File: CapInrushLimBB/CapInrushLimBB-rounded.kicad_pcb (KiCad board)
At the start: 2 copper layers, 56.5 x 34.9 mm, 29 parts, among them J1 Screw_Terminal_01x02, J2 Screw_Terminal_01x02, K1 G5LE-1A, Q1 MPSA42, Q2 IRF9540N, Q3 MPSA42, Q4 BSP230 300V 0.21A

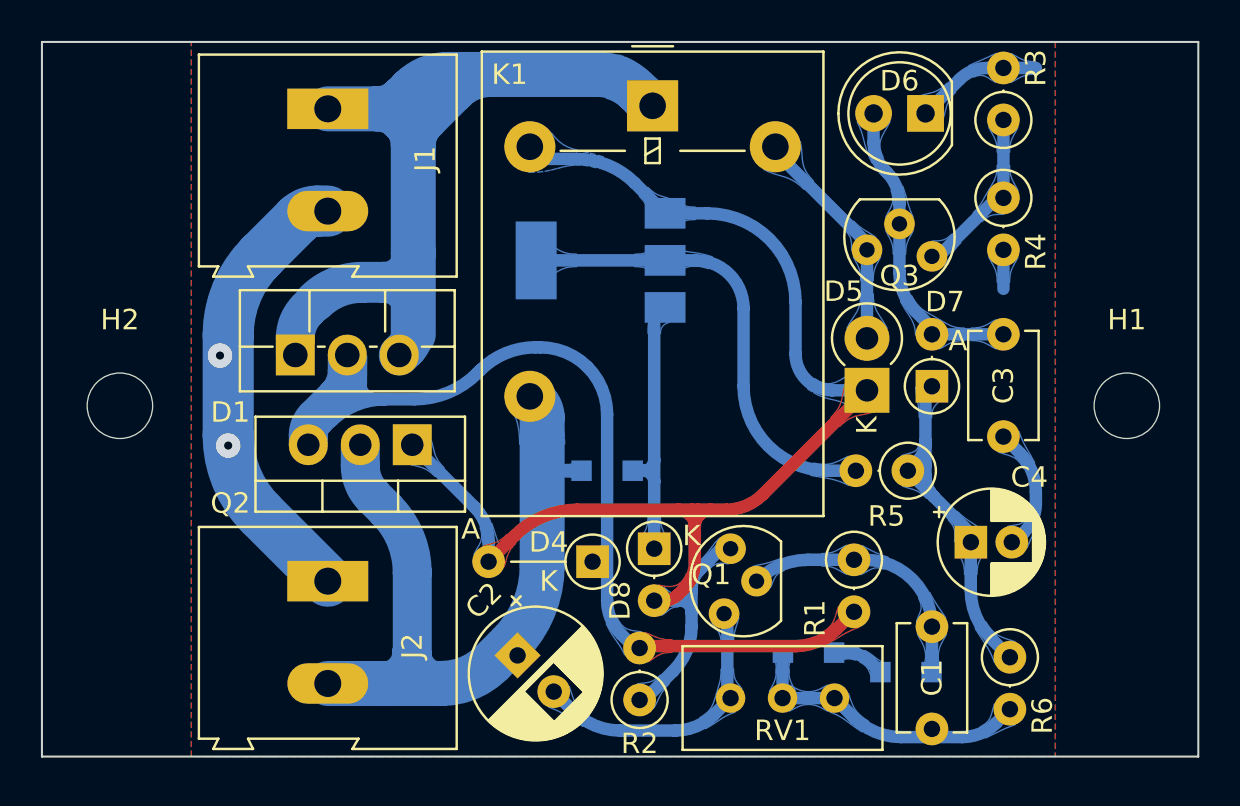
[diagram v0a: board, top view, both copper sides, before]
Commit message: Updated PCB layout of lower voltage capable inrush limiter.
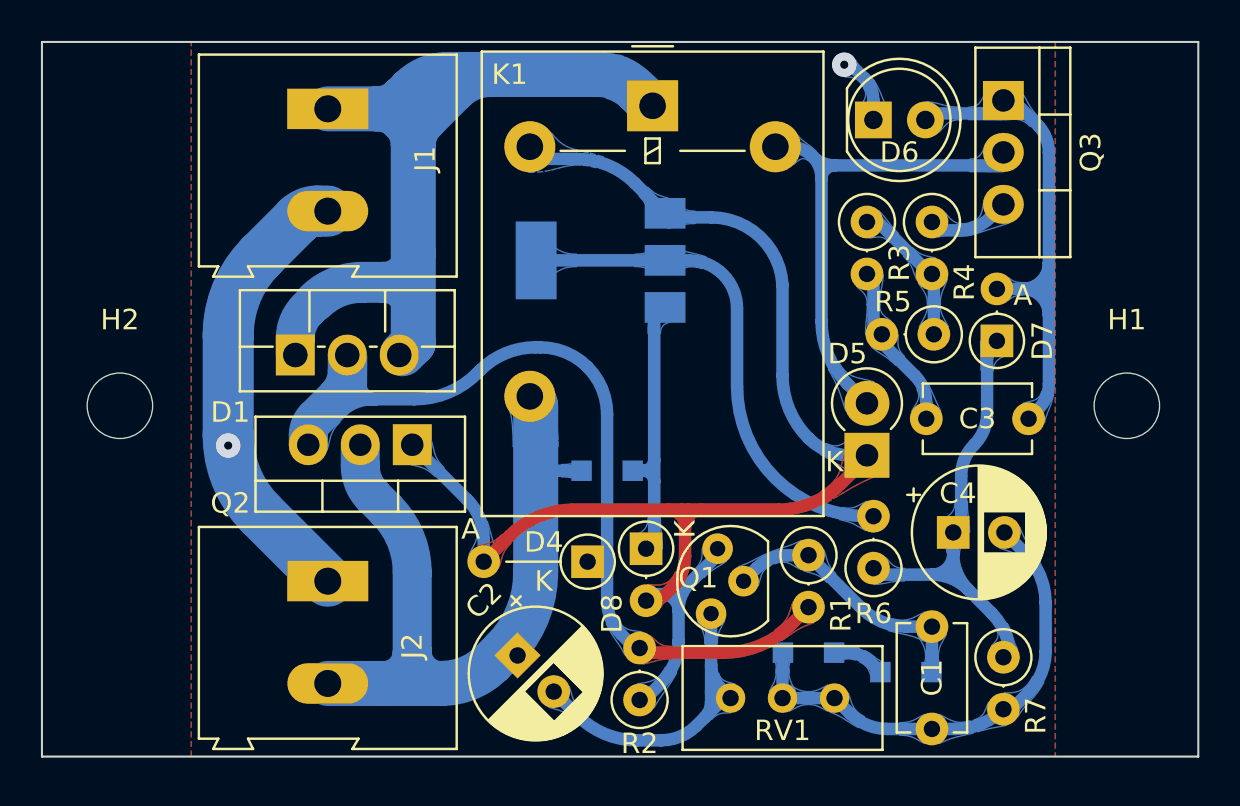
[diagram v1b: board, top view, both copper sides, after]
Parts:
- added R4: 0R, Resistor_THT:R_Axial_DIN0207_L6.3mm_D2.5mm_P2.54mm_Vertical, F.Cu at (250.5, 134.2)
- C4: value 10uF 63V -> 100uF 35V; footprint Capacitor_THT:CP_Radial_D5.0mm_P2.00mm -> Capacitor_THT:CP_Radial_D6.3mm_P2.50mm
- Q3: value MPSA42 -> TIP41C; footprint CapInrushLim:TO-92_Inline -> Package_TO_SOT_THT:TO-220-3_Vertical
- R1: value 100k -> 43k
- R3: value 1k5 -> 220R
- R5: renamed from R4; value 100R -> 110R
- R6: renamed from R5; value 100k -> 10k
- R7: renamed from R6; value 200k -> 100k
- moved R3 8.33 mm to (247.3, 134.2), turned to -90 degrees
- moved Q3 7.68 mm to (254.0, 128.3), turned to -90 degrees
- moved R5 7.48 mm to (250.6, 139.7), turned to 180 degrees
- moved R6 5.05 mm to (247.7, 151.1), turned to 90 degrees
- moved D7 3.87 mm to (253.7, 140.0)
- moved C3 3.87 mm to (250.2, 143.8), turned to 0 degrees
- moved D5 3.18 mm to (247.3, 145.6)
- moved D6 2.57 mm to (247.6, 129.2), turned to 0 degrees
- moved R1 2.23 mm to (244.5, 150.5)
- moved C4 0.99 mm to (251.5, 149.4)
- moved Q1 0.64 mm to (240.7, 153.0)
- moved D8 0.40 mm to (236.5, 150.2)
- moved R7 0.32 mm to (254.0, 155.5)
- moved D4 0.24 mm to (233.7, 150.8)
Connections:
- Q3 pad 1: Net-(Q3-Pad1) -> Net-(C3-Pad2)
- Q3 pad 2: Net-(C3-Pad2) -> /RLCoilLow
- Q3 pad 3: /RLCoilLow -> Net-(Q3-Pad3)
- R3 pad 1: Net-(Q3-Pad1) -> Net-(R3-Pad1)
- R5 pad 1: Net-(Q3-Pad1) -> Net-(R3-Pad1)
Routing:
- net /RLCoilLow: track 11.2 -> 25.8 mm
- net Net-(C3-Pad2): track 14.4 -> 27.1 mm
- net Net-(Q3-Pad1): track 8.37 -> 0.00 mm
- net Net-(R3-Pad1): track 0.00 -> 6.97 mm
- net /Gnd: track 50.9 -> 56.9 mm
- net Net-(C4-Pad1): track 18.8 -> 23.3 mm
- net Net-(Q3-Pad3): track 0.00 -> 4.23 mm
- net Net-(C2-Pad2): track 14.0 -> 18.1 mm
- net Net-(Q4-Pad2): track 22.9 -> 24.6 mm
- net /RLCoilHigh: track 72.7 -> 74.0 mm
- net /RL_Input: track 50.8 -> 49.6 mm
- net /RL_Output: track 38.2 -> 39.1 mm

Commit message: Updated layout and rounded tracks version.
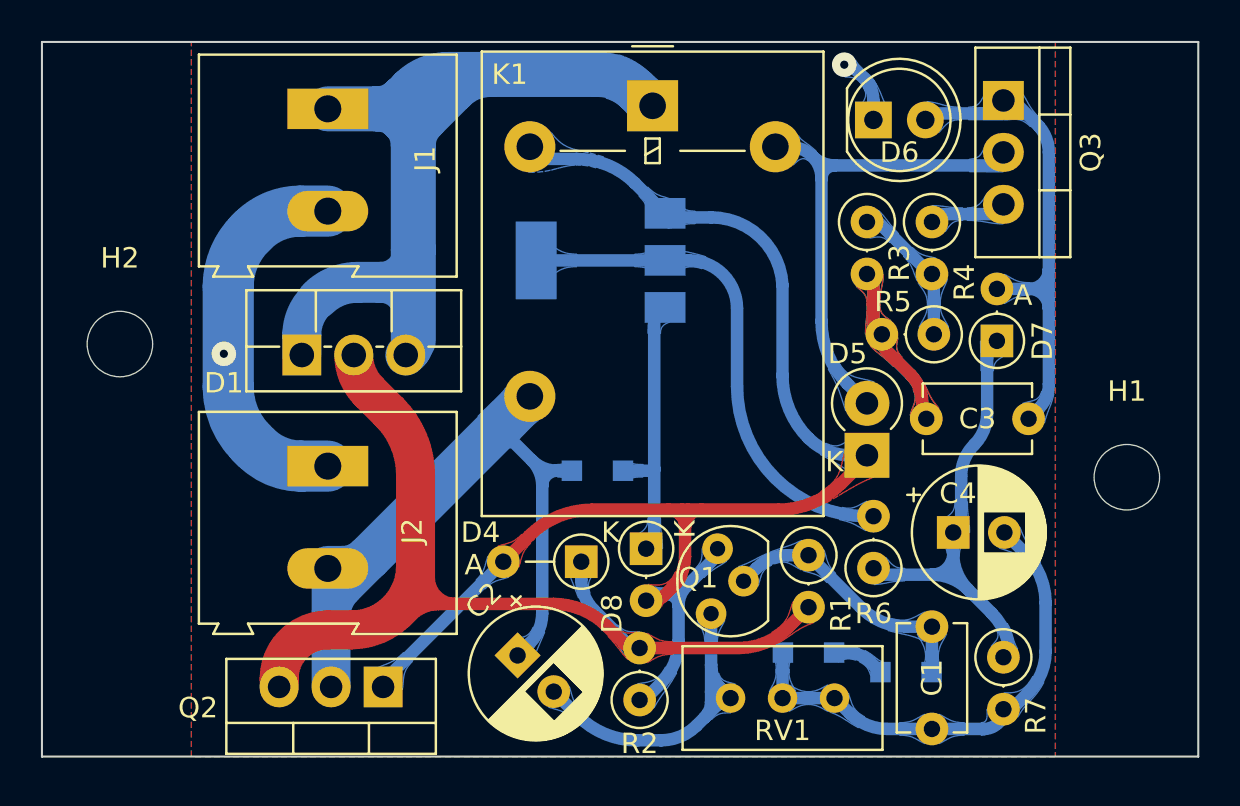
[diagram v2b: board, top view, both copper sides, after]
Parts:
- D4: footprint Diode_THT:D_DO-35_SOD27_P5.08mm_Vertical_AnodeUp -> Diode_THT:D_DO-35_SOD27_P3.81mm_Vertical_AnodeUp
- moved Q2 11.9 mm to (223.7, 156.9)
- moved J2 5.62 mm to (221.0, 146.1)
- moved H1 3.49 mm to (260.0, 146.7)
- moved H2 3.02 mm to (210.8, 140.2)
- moved D9 0.47 mm to (234.2, 146.4)
- moved D1 0.32 mm to (219.7, 140.7)
- moved D4 0.31 mm to (233.4, 150.8)
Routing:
- net /Gnd: track 56.9 -> 61.5 mm
- net /PolProtect: track 49.7 -> 52.4 mm
- net Net-(C3-Pad2): track 27.1 -> 24.5 mm
- net /RL_Input: track 49.6 -> 51.1 mm
- net /RL_Output: track 39.1 -> 40.0 mm
- net Net-(Q3-Pad3): track 4.23 -> 3.50 mm
- net Net-(D8-Pad1): track 14.1 -> 13.6 mm

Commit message: Changed the reference type, changed current set resistor strategy and updated PCB.
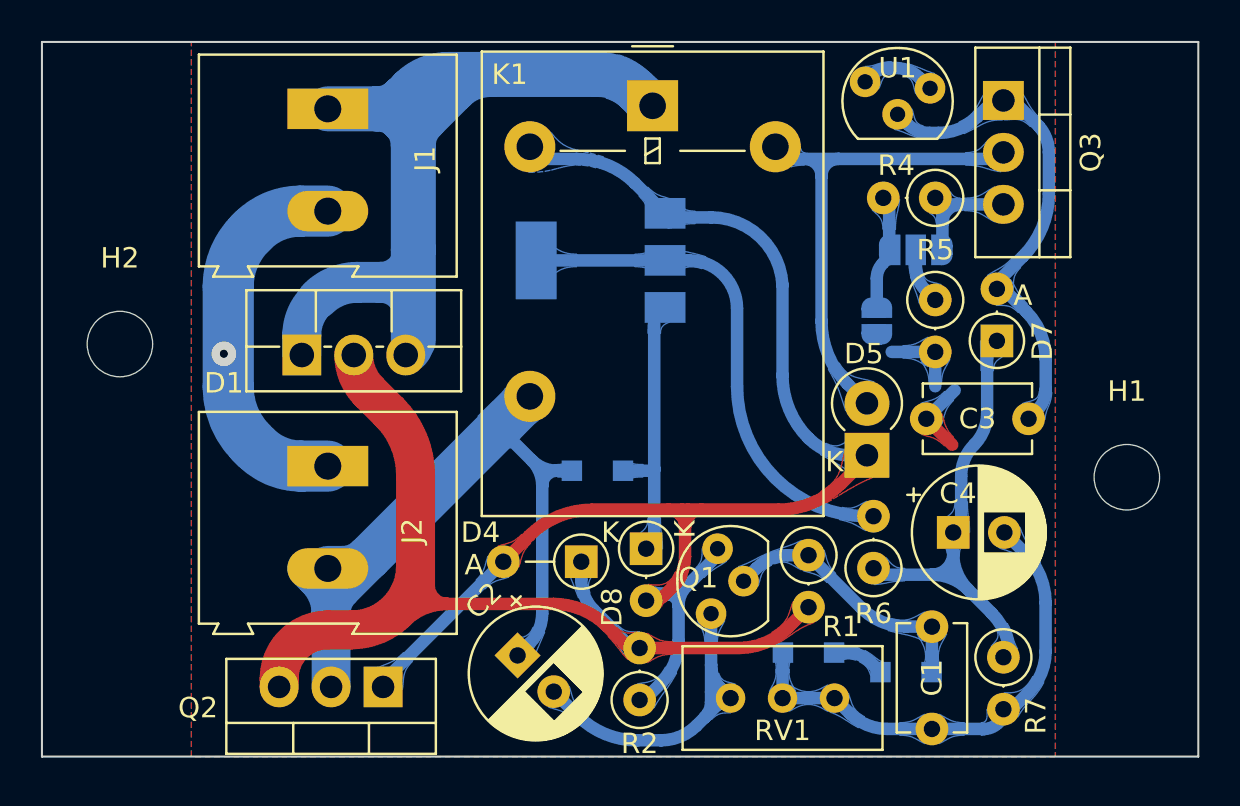
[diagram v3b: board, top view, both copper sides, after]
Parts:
- removed D6: Red LED, LED_THT:LED_D5.0mm
- removed R3: 220R, Resistor_THT:R_Axial_DIN0207_L6.3mm_D2.5mm_P2.54mm_Vertical
- added JP1: SolderJumper_3_Open, Jumper:SolderJumper-3_P1.3mm_Open_RoundedPad1.0x1.5mm, B.Cu at (249.7, 135.6)
- added JP2: SolderJumper_2_Open, Jumper:SolderJumper-2_P1.3mm_Open_RoundedPad1.0x1.5mm, B.Cu at (247.8, 139.1)
- added U1: LM385Z-ADJ, CapInrushLim:TO-92_Inline, F.Cu at (247.6, 128.3)
- R4: value 0R -> 47
- R5: value 110R -> 47
- moved R5 1.68 mm to (250.7, 138.0), turned to -90 degrees
- moved R4 1.19 mm to (250.7, 133.0), turned to 180 degrees
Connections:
- R4 pad 2: Net-(R3-Pad1) -> Net-(JP1-Pad1)
- R5 pad 1: Net-(R3-Pad1) -> Net-(JP1-Pad2)
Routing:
- net /Gnd: track 61.5 -> 54.5 mm, vias 2 -> 1
- net Net-(R3-Pad1): track 6.97 -> 0.00 mm
- net Net-(JP1-Pad1): track 0.00 -> 5.23 mm
- net Net-(JP1-Pad3): track 3.50 -> 7.04 mm
- net Net-(JP1-Pad2): track 0.00 -> 2.76 mm
- net /RL_Output: track 40.0 -> 38.8 mm
- net Net-(C3-Pad2): track 24.5 -> 23.9 mm

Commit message: Updated rounded tracks version.
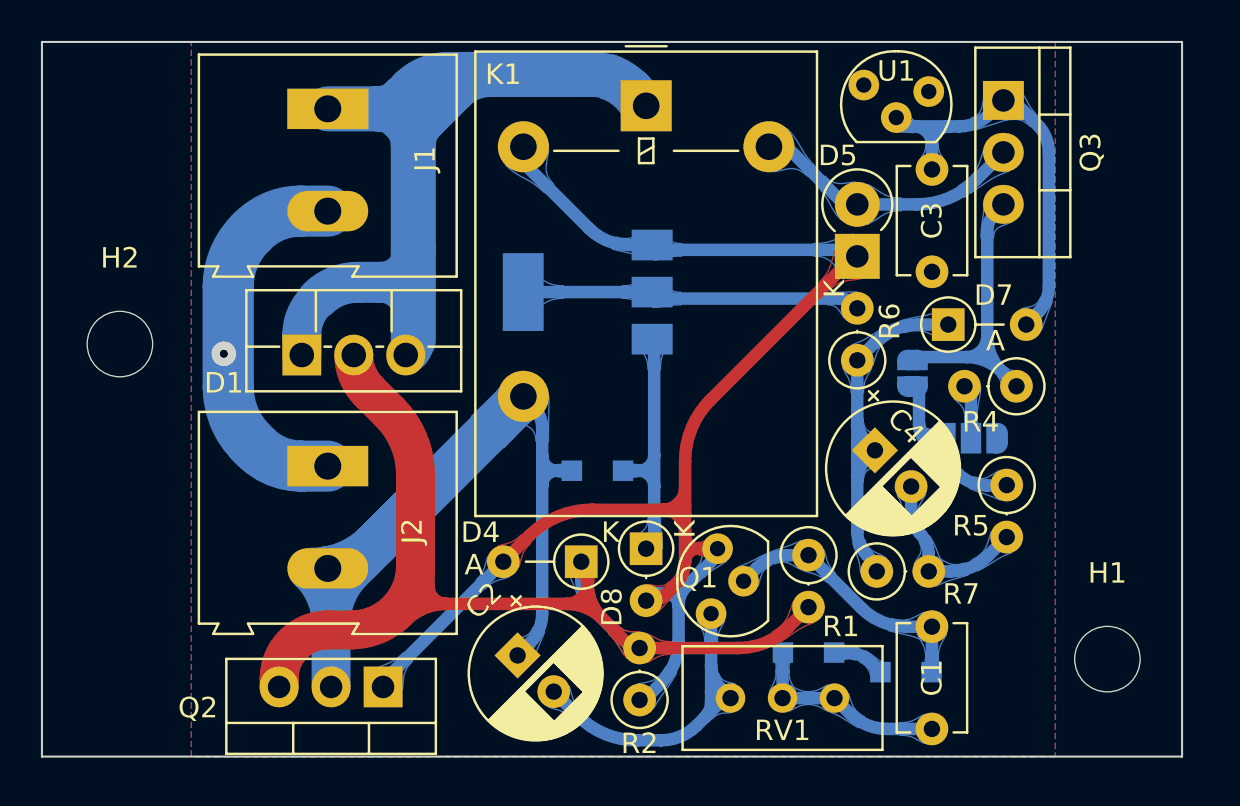
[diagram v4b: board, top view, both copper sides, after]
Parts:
- D7: footprint Diode_THT:D_DO-35_SOD27_P2.54mm_Vertical_AnodeUp -> Diode_THT:D_DO-35_SOD27_P3.81mm_Vertical_AnodeUp
- moved R6 10.2 mm to (246.9, 141.0)
- moved R4 10.0 mm to (254.6, 142.2)
- moved D5 9.73 mm to (246.9, 135.9)
- moved R5 9.70 mm to (254.2, 147.1)
- moved JP1 9.59 mm to (252.4, 144.8)
- moved H1 8.94 mm to (259.1, 155.6)
- moved R7 7.48 mm to (247.8, 151.3), turned to 0 degrees
- moved C3 7.19 mm to (250.5, 136.6), turned to 90 degrees
- moved C4 5.54 mm to (247.7, 145.4), turned to -45 degrees
- moved JP2 3.09 mm to (249.6, 141.6), turned to -90 degrees
- moved D7 2.51 mm to (251.3, 139.2), turned to 0 degrees
- moved Q4 1.67 mm to (233.7, 137.6)
- moved K1 0.31 mm to (236.5, 128.5)
- moved U1 0.17 mm to (247.5, 128.5)
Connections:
- JP1 pad 3: Net-(JP1-Pad3) -> /Gnd
- JP2 pad 1: /Gnd -> Net-(JP2-Pad1)
- Q3 pad 3: Net-(JP1-Pad3) -> Net-(JP2-Pad1)
- R4 pad 1: Net-(JP1-Pad3) -> Net-(JP2-Pad1)
- R4 pad 2: Net-(JP1-Pad1) -> Net-(JP1-Pad2)
- R5 pad 1: Net-(JP1-Pad2) -> Net-(JP1-Pad1)
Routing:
- net /Gnd: track 54.5 -> 37.7 mm
- net Net-(JP2-Pad1): track 0.00 -> 15.8 mm
- net /RLCoilLow: track 25.8 -> 12.2 mm
- net /RL_Output: track 38.8 -> 50.1 mm
- net Net-(Q4-Pad2): track 24.6 -> 16.0 mm
- net Net-(JP1-Pad3): track 7.04 -> 0.00 mm
- net Net-(JP1-Pad1): track 5.23 -> 10.3 mm
- net /PolProtect: track 52.9 -> 57.2 mm
- net Net-(C4-Pad1): track 23.3 -> 20.0 mm
- net Net-(C3-Pad2): track 23.9 -> 21.5 mm
- net /RLCoilHigh: track 74.1 -> 75.8 mm
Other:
- board size 56.5 x 34.9 mm -> 55.7 x 34.9 mm

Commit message: Updated values of relay current limiter resistors.
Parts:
- R4: value 47 -> 560
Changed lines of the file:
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@@
       (effects (font (size 1 1) (thickness 0.15)))
     )
-    (fp_text value "47" (at 1.27 2.37) (layer "F.Fab")
+    (fp_text value "560" (at 1.27 2.37) (layer "F.Fab")
       (effects (font (size 1 1) (thickness 0.15)))
     )

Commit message: Updating model, schematic and PCB to remove cap. on the relay timer ref. and to fit a zener across the relay coil.
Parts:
- C3: value 100nF 50V -> 100nF 50V (DNF)
- D5: value 1n4002 -> 1N4749A (24V)
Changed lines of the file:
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@@
       (effects (font (size 1 1) (thickness 0.15)))
     )
-    (fp_text value "1n4002" (at 1.27 3.639635 90) (layer "F.Fab")
+    (fp_text value "1N4749A (24V)" (at 1.27 3.639635 90) (layer "F.Fab")
       (effects (font (size 1 1) (thickness 0.15)))
     )
@@
       (effects (font (size 1 1) (thickness 0.15)))
     )
-    (fp_text value "100nF 50V" (at 2.5 2.85 90) (layer "F.Fab")
+    (fp_text value "100nF 50V (DNF)" (at 2.5 2.85 90) (layer "F.Fab")
       (effects (font (size 1 1) (thickness 0.15)))
     )

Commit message: Updated layout on original and rounded designs.
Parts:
- D5: value 1N4749A (24V) -> BZX55C24; footprint Diode_THT:D_DO-41_SOD81_P2.54mm_Vertical_KathodeUp -> Diode_THT:D_DO-35_SOD27_P2.54mm_Vertical_KathodeUp
